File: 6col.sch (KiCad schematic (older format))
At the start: 47 parts, among them K1 KEYSW, K10 KEYSW, K11 KEYSW, K12 KEYSW, K13 KEYSW, K14 KEYSW, K15 KEYSW, K16 KEYSW, K17 KEYSW, K18 KEYSW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

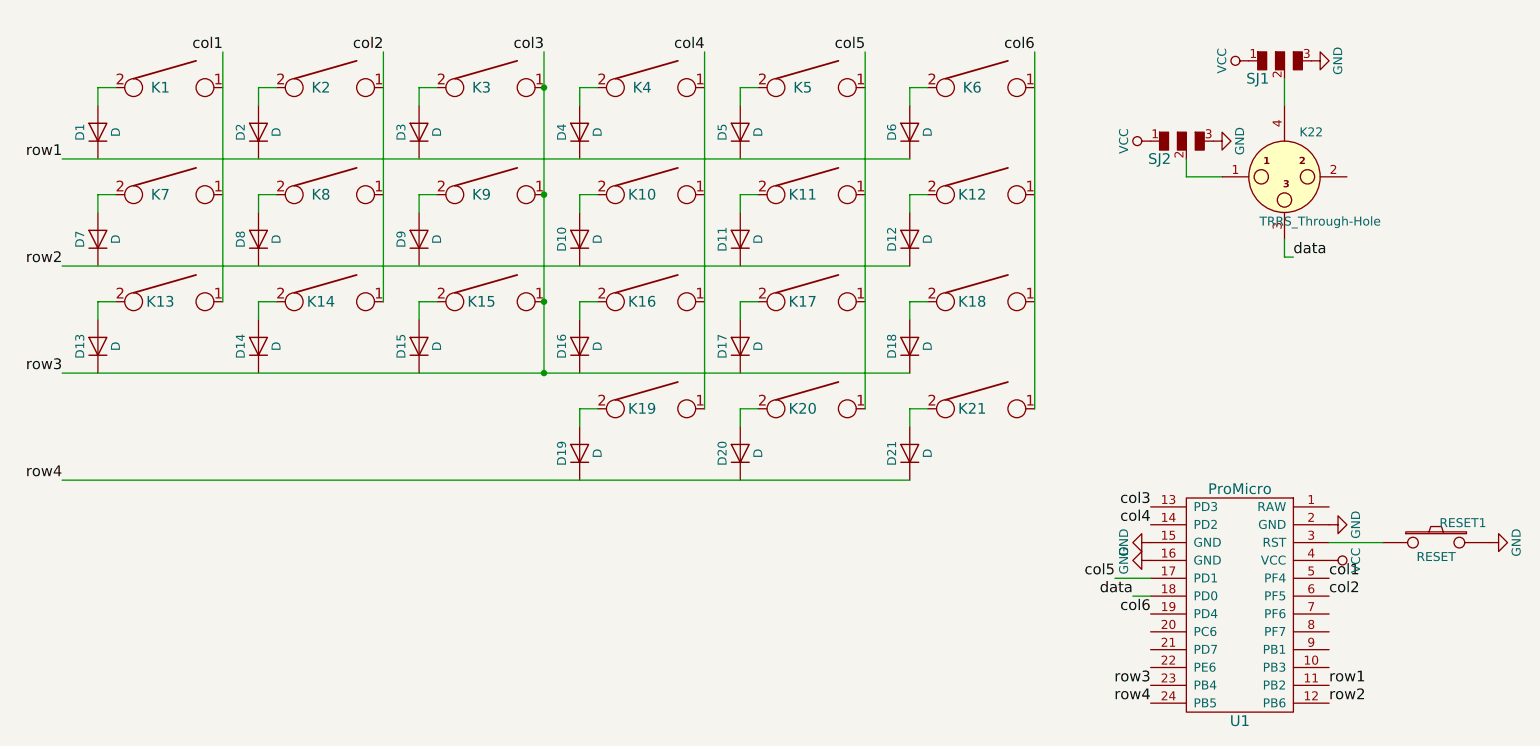
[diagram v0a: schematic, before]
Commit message: Fix short on sch between c3 and r3
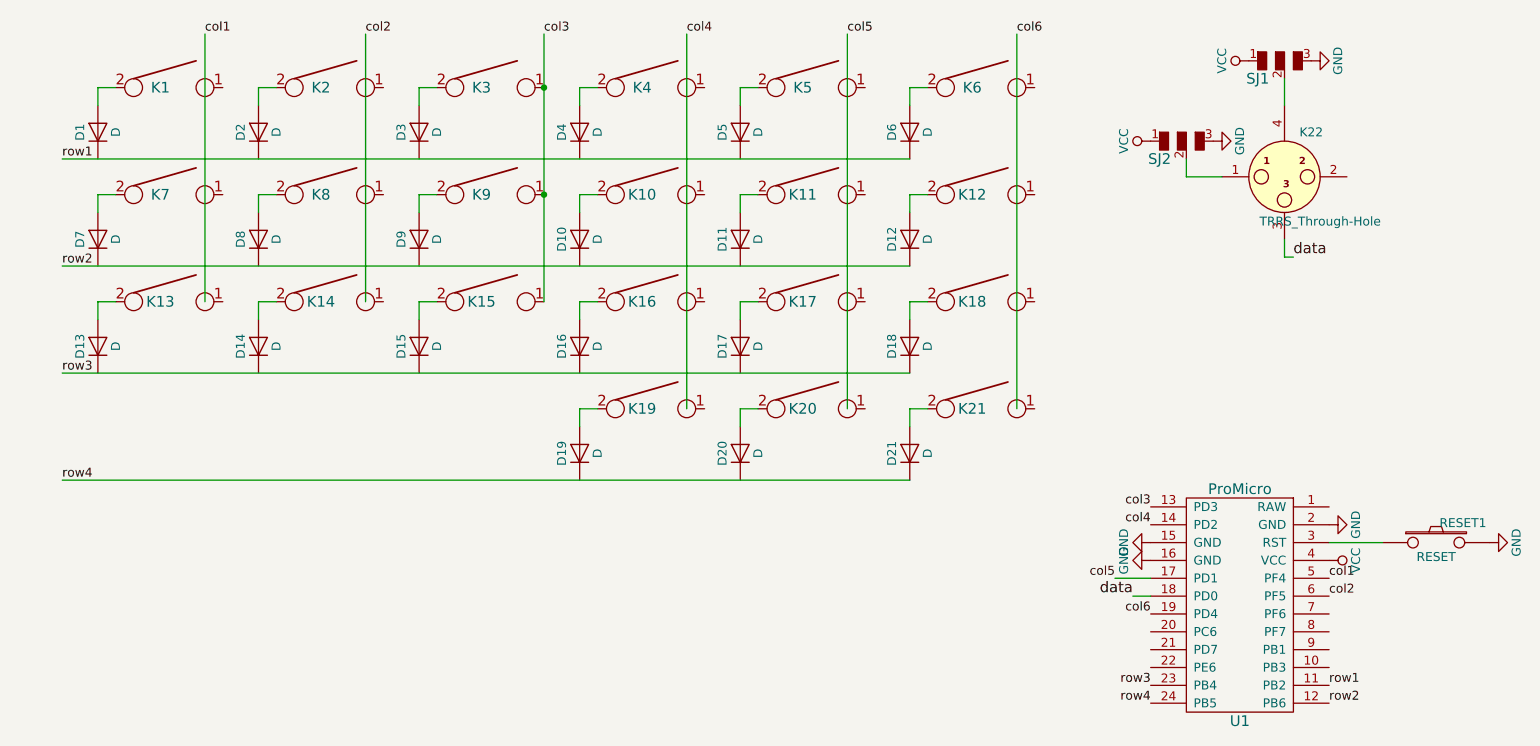
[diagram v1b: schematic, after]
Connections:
- wire segments 64 -> 62
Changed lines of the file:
@@
 $EndDescr
-$Comp
-L ProMicro:ProMicro U1
-U 1 1 588E2344
-P 8300 4650
-F 0 "U1" H 8300 3800 60  0000 C CNN
-F 1 "ProMicro" H 8300 5100 60  0000 C CNN
-F 2 "canadian_footprints:Pro_Micro" H 8300 4650 60  0001 C CNN
-F 3 "" H 8300 4650 60  0001 C CNN
-	1    8300 4650
-	1    0    0    -1
-$EndComp
 $Comp
 L canadian_parts:KEYSW K1
@@
 	0    -1   -1   0
 $EndComp
-Wire Wire Line
-	1900 2050 1900 1950
-Wire Wire Line
-	1900 1950 2000 1950
-Wire Wire Line
-	2800 2050 2800 1950
-Wire Wire Line
-	2800 1950 2900 1950
-Wire Wire Line
-	3700 2050 3700 1950
-Wire Wire Line
-	3700 1950 3800 1950
-Wire Wire Line
-	4600 2050 4600 1950
-Wire Wire Line
-	4600 1950 4700 1950
-Wire Wire Line
-	4600 2650 4600 2550
-Wire Wire Line
-	4600 2550 4700 2550
-Wire Wire Line
-	3700 2650 3700 2550
-Wire Wire Line
-	3700 2550 3800 2550
-Wire Wire Line
-	2800 2650 2800 2550
-Wire Wire Line
-	2800 2550 2900 2550
-Wire Wire Line
-	1900 2650 1900 2550
-Wire Wire Line
-	1900 2550 2000 2550
-Wire Wire Line
-	1900 3150 2000 3150
-Wire Wire Line
-	2800 3250 2800 3150
-Wire Wire Line
-	2800 3150 2900 3150
-Wire Wire Line
-	3700 3250 3700 3150
-Wire Wire Line
-	3700 3150 3800 3150
-Wire Wire Line
-	4600 3250 4600 3150
-Wire Wire Line
-	4600 3150 4700 3150
-Wire Wire Line
-	4600 3850 4600 3750
-Wire Wire Line
-	4600 3750 4700 3750
-Text Label 2600 1750 2    60   ~ 0
-col1
-Text Label 3500 1750 2    60   ~ 0
-col2
-Text Label 4400 1750 2    60   ~ 0
-col3
-Text Label 5300 1750 2    60   ~ 0
-col4
-Text Label 1700 2350 2    60   ~ 0
-row1
-Text Label 1700 2950 2    60   ~ 0
-row2
-Text Label 1700 3550 2    60   ~ 0
-row3
-Text Label 1700 4150 2    60   ~ 0
-row4
 $Comp
 L canadian_parts:SOLDER_JUMPER_3 SJ2
@@
 	1    0    0    -1
 $EndComp
-Wire Wire Line
-	8550 1900 8550 2050
-Wire Wire Line
-	8200 2450 8000 2450
-Wire Wire Line
-	8000 2450 8000 2350
 $Comp
 L power:GND #PWR01
@@
 Text Label 8600 2900 0    60   ~ 0
 data
-Wire Wire Line
-	8550 2800 8550 2900
-Wire Wire Line
-	8550 2900 8600 2900
 Text Label 7700 4800 2    60   ~ 0
 data
-Wire Wire Line
-	7700 4800 7800 4800
-Text Label 8800 4700 0    60   ~ 0
-col1
-Text Label 7800 4400 2    60   ~ 0
-col4
-Text Label 7600 4700 2    60   ~ 0
-col5
-Text Label 7800 4900 2    60   ~ 0
-col6
-Text Label 8800 5300 0    60   ~ 0
-row1
-Text Label 8800 5400 0    60   ~ 0
-row2
-Text Label 7800 5300 2    60   ~ 0
-row3
-Text Label 7800 5400 2    60   ~ 0
-row4
-Text Label 7800 4300 2    60   ~ 0
-col3
-Wire Wire Line
-	7600 4700 7800 4700
 $Comp
 L keyboard_parts:SW_PUSH RESET1
@@
 	0    -1   -1   0
 $EndComp
-Wire Wire Line
-	9100 4500 8800 4500
-Wire Wire Line
-	2600 1750 2600 3150
-Wire Wire Line
-	3500 1750 3500 3150
-Wire Wire Line
-	5300 1750 5300 3750
-Wire Wire Line
-	1900 3250 1900 3150
 $Comp
 L Device:D D13
@@
 	0    -1   -1   0
 $EndComp
-Text Label 8800 4800 0    60   ~ 0
-col2
-Wire Wire Line
-	6200 1750 6200 3750
-Text Label 6200 1750 2    60   ~ 0
-col5
-Wire Wire Line
-	5500 3750 5600 3750
-Wire Wire Line
-	5500 3850 5500 3750
-Wire Wire Line
-	5500 3150 5600 3150
-Wire Wire Line
-	5500 3250 5500 3150
-Wire Wire Line
-	5500 2550 5600 2550
-Wire Wire Line
-	5500 2650 5500 2550
-Wire Wire Line
-	5500 1950 5600 1950
-Wire Wire Line
-	5500 2050 5500 1950
 $Comp
 L Device:D D20
@@
 	1    0    0    -1
 $EndComp
-Wire Wire Line
-	7150 1750 7150 3750
-Text Label 7150 1750 2    60   ~ 0
-col6
-Wire Wire Line
-	6450 3750 6550 3750
-Wire Wire Line
-	6450 3850 6450 3750
-Wire Wire Line
-	6450 3150 6550 3150
-Wire Wire Line
-	6450 3250 6450 3150
-Wire Wire Line
-	6450 2550 6550 2550
-Wire Wire Line
-	6450 2650 6450 2550
-Wire Wire Line
-	6450 1950 6550 1950
-Wire Wire Line
-	6450 2050 6450 1950
 $Comp
 L Device:D D21
@@
 	1    0    0    -1
 $EndComp
-Wire Wire Line
-	1700 3550 4400 3550
-Wire Wire Line
-	1700 2950 6450 2950
-Wire Wire Line
-	1700 2350 6450 2350
-Wire Wire Line
-	1700 4150 6450 4150
-Wire Wire Line
-	4400 1750 4400 1950
-Connection ~ 4400 1950
-Wire Wire Line
-	4400 1950 4400 2550
-Connection ~ 4400 2550
-Wire Wire Line
-	4400 2550 4400 3150
-Connection ~ 4400 3150
-Wire Wire Line
-	4400 3150 4400 3550
-Connection ~ 4400 3550
-Wire Wire Line
-	4400 3550 6450 3550
 $Comp
 L canadian_parts:TRRS_Through-Hole K22
@@
 	1    0    0    -1
 $EndComp
+$Comp
+L ProMicro:ProMicro U1
+U 1 1 588E2344
+P 8300 4650
+F 0 "U1" H 8300 3800 60  0000 C CNN
+F 1 "ProMicro" H 8300 5100 60  0000 C CNN
+F 2 "canadian_footprints:Pro_Micro" H 8300 4650 60  0001 C CNN
+F 3 "" H 8300 4650 60  0001 C CNN
+	1    8300 4650
+	1    0    0    -1
+$EndComp
+Text Label 8800 5300 0    50   ~ 0
+row1
+Text Label 8800 5400 0    50   ~ 0
+row2
+Text Label 7800 5300 2    50   ~ 0
+row3
+Text Label 7800 5400 2    50   ~ 0
+row4
+Text Label 1700 2350 0    50   ~ 0
+row1
+Text Label 1700 2950 0    50   ~ 0
+row2
+Text Label 1700 3550 0    50   ~ 0
+row3
+Text Label 1700 4150 0    50   ~ 0
+row4
+Text Label 2500 1650 0    50   ~ 0
+col1
+Text Label 3400 1650 0    50   ~ 0
+col2
+Text Label 5200 1650 0    50   ~ 0
+col4
+Text Label 6100 1650 0    50   ~ 0
+col5
+Text Label 7050 1650 0    50   ~ 0
+col6
+Text Label 4400 1650 0    50   ~ 0
+col3
+Text Label 8800 4700 0    50   ~ 0
+col1
+Text Label 8800 4800 0    50   ~ 0
+col2
+Wire Wire Line
+	1900 2050 1900 1950
+Wire Wire Line
+	1900 1950 2000 1950
+Wire Wire Line
+	2800 2050 2800 1950
+Wire Wire Line
+	2800 1950 2900 1950
+Wire Wire Line
+	3700 2050 3700 1950
+Wire Wire Line
+	3700 1950 3800 1950
+Wire Wire Line
+	4600 2050 4600 1950
+Wire Wire Line
+	4600 1950 4700 1950
+Wire Wire Line
+	4600 2650 4600 2550
+Wire Wire Line
+	4600 2550 4700 2550
+Wire Wire Line
+	3700 2650 3700 2550
+Wire Wire Line
+	3700 2550 3800 2550
+Wire Wire Line
+	2800 2650 2800 2550
+Wire Wire Line
+	2800 2550 2900 2550
+Wire Wire Line
+	1900 2650 1900 2550
+Wire Wire Line
+	1900 2550 2000 2550
+Wire Wire Line
+	1900 3150 2000 3150
+Wire Wire Line
+	2800 3250 2800 3150
+Wire Wire Line
+	2800 3150 2900 3150
+Wire Wire Line
+	3700 3250 3700 3150
+Wire Wire Line
+	3700 3150 3800 3150
+Wire Wire Line
+	4600 3250 4600 3150
+Wire Wire Line
+	4600 3150 4700 3150
+Wire Wire Line
+	4600 3850 4600 3750
+Wire Wire Line
+	4600 3750 4700 3750
+Wire Wire Line
+	8550 1900 8550 2050
+Wire Wire Line
+	8200 2450 8000 2450
+Wire Wire Line
+	8000 2450 8000 2350
+Wire Wire Line
+	8550 2800 8550 2900
+Wire Wire Line
+	8550 2900 8600 2900
+Wire Wire Line
+	7700 4800 7800 4800
+Wire Wire Line
+	7600 4700 7800 4700
+Wire Wire Line
+	9100 4500 8800 4500
+Wire Wire Line
+	1900 3250 1900 3150
+Wire Wire Line
+	5500 3750 5600 3750
+Wire Wire Line
+	5500 3850 5500 3750
+Wire Wire Line
+	5500 3150 5600 3150
+Wire Wire Line
+	5500 3250 5500 3150
+Wire Wire Line
+	5500 2550 5600 2550
+Wire Wire Line
+	5500 2650 5500 2550
+Wire Wire Line
+	5500 1950 5600 1950
+Wire Wire Line
+	5500 2050 5500 1950
+Wire Wire Line
+	6450 3750 6550 3750
+Wire Wire Line
+	6450 3850 6450 3750
+Wire Wire Line
+	6450 3150 6550 3150
+Wire Wire Line
+	6450 3250 6450 3150
+Wire Wire Line
+	6450 2550 6550 2550
+Wire Wire Line
+	6450 2650 6450 2550
+Wire Wire Line
+	6450 1950 6550 1950
+Wire Wire Line
+	6450 2050 6450 1950
+Wire Wire Line
+	1700 2950 6450 2950
+Wire Wire Line
+	1700 2350 6450 2350
+Wire Wire Line
+	1700 4150 6450 4150
+Wire Wire Line
+	4400 1950 4400 2550
+Connection ~ 4400 2550
+Wire Wire Line
+	4400 2550 4400 3150
+Wire Wire Line
+	2500 3150 2500 1650
+Wire Wire Line
+	3400 3150 3400 1650
+Wire Wire Line
+	6100 3750 6100 1650
+Wire Wire Line
+	7050 3750 7050 1650
+Wire Wire Line
+	5200 3750 5200 1650
+Wire Wire Line
+	4400 1950 4400 1650
+Connection ~ 4400 1950
+Text Label 7800 4300 2    50   ~ 0
+col3
+Text Label 7800 4400 2    50   ~ 0
+col4
+Text Label 7600 4700 2    50   ~ 0
+col5
+Text Label 7800 4900 2    50   ~ 0
+col6
+Wire Wire Line
+	1700 3550 6450 3550
 $EndSCHEMATC

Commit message: Fix sch again
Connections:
- wire segments 62 -> 90
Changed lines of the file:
@@
 	1    0    0    -1
 $EndComp
-Text Label 8800 5300 0    50   ~ 0
+Text Label 7800 5300 2    60   ~ 0
+row3
+Text Label 1700 2350 2    60   ~ 0
 row1
-Text Label 8800 5400 0    50   ~ 0
+Text Label 1700 2950 2    60   ~ 0
 row2
-Text Label 7800 5300 2    50   ~ 0
+Text Label 1700 3550 2    60   ~ 0
 row3
-Text Label 7800 5400 2    50   ~ 0
+Text Label 1700 4150 2    60   ~ 0
 row4
-Text Label 1700 2350 0    50   ~ 0
+Text Label 2600 1650 0    60   ~ 0
+col1
+Text Label 3500 1650 0    60   ~ 0
+col2
+Text Label 5300 1650 0    60   ~ 0
+col4
+Text Label 6200 1650 0    60   ~ 0
+col5
+Text Label 7150 1650 0    60   ~ 0
+col6
+Text Label 4400 1650 0    60   ~ 0
+col3
+Wire Wire Line
+	1900 2050 1900 1950
+Wire Wire Line
+	1900 1950 2000 1950
+Wire Wire Line
+	2800 2050 2800 1950
+Wire Wire Line
+	2800 1950 2900 1950
+Wire Wire Line
+	3700 2050 3700 1950
+Wire Wire Line
+	3700 1950 3800 1950
+Wire Wire Line
+	4600 2050 4600 1950
+Wire Wire Line
+	4600 1950 4700 1950
+Wire Wire Line
+	4600 2650 4600 2550
+Wire Wire Line
+	4600 2550 4700 2550
+Wire Wire Line
+	3700 2650 3700 2550
+Wire Wire Line
+	3700 2550 3800 2550
+Wire Wire Line
+	2800 2650 2800 2550
+Wire Wire Line
+	2800 2550 2900 2550
+Wire Wire Line
+	1900 2650 1900 2550
+Wire Wire Line
+	1900 2550 2000 2550
+Wire Wire Line
+	1900 3150 2000 3150
+Wire Wire Line
+	2800 3250 2800 3150
+Wire Wire Line
+	2800 3150 2900 3150
+Wire Wire Line
+	3700 3250 3700 3150
+Wire Wire Line
+	3700 3150 3800 3150
+Wire Wire Line
+	4600 3250 4600 3150
+Wire Wire Line
+	4600 3150 4700 3150
+Wire Wire Line
+	4600 3850 4600 3750
+Wire Wire Line
+	4600 3750 4700 3750
+Wire Wire Line
+	8550 1900 8550 2050
+Wire Wire Line
+	8200 2450 8000 2450
+Wire Wire Line
+	8000 2450 8000 2350
+Wire Wire Line
+	8550 2800 8550 2900
+Wire Wire Line
+	8550 2900 8600 2900
+Wire Wire Line
+	7700 4800 7800 4800
+Wire Wire Line
+	7600 4700 7800 4700
+Wire Wire Line
+	9100 4500 8800 4500
+Wire Wire Line
+	1900 3250 1900 3150
+Wire Wire Line
+	5500 3750 5600 3750
+Wire Wire Line
+	5500 3850 5500 3750
+Wire Wire Line
+	5500 3150 5600 3150
+Wire Wire Line
+	5500 3250 5500 3150
+Wire Wire Line
+	5500 2550 5600 2550
+Wire Wire Line
+	5500 2650 5500 2550
+Wire Wire Line
+	5500 1950 5600 1950
+Wire Wire Line
+	5500 2050 5500 1950
+Wire Wire Line
+	6450 3750 6550 3750
+Wire Wire Line
+	6450 3850 6450 3750
+Wire Wire Line
+	6450 3150 6550 3150
+Wire Wire Line
+	6450 3250 6450 3150
+Wire Wire Line
+	6450 2550 6550 2550
+Wire Wire Line
+	6450 2650 6450 2550
+Wire Wire Line
+	6450 1950 6550 1950
+Wire Wire Line
+	6450 2050 6450 1950
+Wire Wire Line
+	1700 2950 1900 2950
+Wire Wire Line
+	1700 2350 1900 2350
+Wire Wire Line
+	1700 4150 4600 4150
+Text Label 7800 4300 2    60   ~ 0
+col3
+Text Label 7800 4400 2    60   ~ 0
+col4
+Text Label 7600 4700 2    60   ~ 0
+col5
+Text Label 7800 4900 2    60   ~ 0
+col6
+Wire Wire Line
+	1700 3550 1900 3550
+Wire Wire Line
+	7150 1650 7150 1950
+Wire Wire Line
+	6200 1650 6200 1950
+Wire Wire Line
+	3500 1650 3500 1950
+Wire Wire Line
+	2600 1650 2600 1950
+Text Label 7800 5400 2    60   ~ 0
+row4
+Text Label 8800 4700 0    60   ~ 0
+col1
+Text Label 8800 4800 0    60   ~ 0
+col2
+Text Label 8800 5300 0    60   ~ 0
 row1
-Text Label 1700 2950 0    50   ~ 0
+Text Label 8800 5400 0    60   ~ 0
 row2
-Text Label 1700 3550 0    50   ~ 0
-row3
-Text Label 1700 4150 0    50   ~ 0
-row4
-Text Label 2500 1650 0    50   ~ 0
-col1
-Text Label 3400 1650 0    50   ~ 0
-col2
-Text Label 5200 1650 0    50   ~ 0
-col4
-Text Label 6100 1650 0    50   ~ 0
-col5
-Text Label 7050 1650 0    50   ~ 0
-col6
-Text Label 4400 1650 0    50   ~ 0
-col3
-Text Label 8800 4700 0    50   ~ 0
-col1
-Text Label 8800 4800 0    50   ~ 0
-col2
-Wire Wire Line
-	1900 2050 1900 1950
-Wire Wire Line
-	1900 1950 2000 1950
-Wire Wire Line
-	2800 2050 2800 1950
-Wire Wire Line
-	2800 1950 2900 1950
-Wire Wire Line
-	3700 2050 3700 1950
-Wire Wire Line
-	3700 1950 3800 1950
-Wire Wire Line
-	4600 2050 4600 1950
-Wire Wire Line
-	4600 1950 4700 1950
-Wire Wire Line
-	4600 2650 4600 2550
-Wire Wire Line
-	4600 2550 4700 2550
-Wire Wire Line
-	3700 2650 3700 2550
-Wire Wire Line
-	3700 2550 3800 2550
-Wire Wire Line
-	2800 2650 2800 2550
-Wire Wire Line
-	2800 2550 2900 2550
-Wire Wire Line
-	1900 2650 1900 2550
-Wire Wire Line
-	1900 2550 2000 2550
-Wire Wire Line
-	1900 3150 2000 3150
-Wire Wire Line
-	2800 3250 2800 3150
-Wire Wire Line
-	2800 3150 2900 3150
-Wire Wire Line
-	3700 3250 3700 3150
-Wire Wire Line
-	3700 3150 3800 3150
-Wire Wire Line
-	4600 3250 4600 3150
-Wire Wire Line
-	4600 3150 4700 3150
-Wire Wire Line
-	4600 3850 4600 3750
-Wire Wire Line
-	4600 3750 4700 3750
-Wire Wire Line
-	8550 1900 8550 2050
-Wire Wire Line
-	8200 2450 8000 2450
-Wire Wire Line
-	8000 2450 8000 2350
-Wire Wire Line
-	8550 2800 8550 2900
-Wire Wire Line
-	8550 2900 8600 2900
-Wire Wire Line
-	7700 4800 7800 4800
-Wire Wire Line
-	7600 4700 7800 4700
-Wire Wire Line
-	9100 4500 8800 4500
-Wire Wire Line
-	1900 3250 1900 3150
-Wire Wire Line
-	5500 3750 5600 3750
-Wire Wire Line
-	5500 3850 5500 3750
-Wire Wire Line
-	5500 3150 5600 3150
-Wire Wire Line
-	5500 3250 5500 3150
-Wire Wire Line
-	5500 2550 5600 2550
-Wire Wire Line
-	5500 2650 5500 2550
-Wire Wire Line
-	5500 1950 5600 1950
-Wire Wire Line
-	5500 2050 5500 1950
-Wire Wire Line
-	6450 3750 6550 3750
-Wire Wire Line
-	6450 3850 6450 3750
-Wire Wire Line
-	6450 3150 6550 3150
-Wire Wire Line
-	6450 3250 6450 3150
-Wire Wire Line
-	6450 2550 6550 2550
-Wire Wire Line
-	6450 2650 6450 2550
-Wire Wire Line
-	6450 1950 6550 1950
-Wire Wire Line
-	6450 2050 6450 1950
-Wire Wire Line
-	1700 2950 6450 2950
-Wire Wire Line
-	1700 2350 6450 2350
-Wire Wire Line
-	1700 4150 6450 4150
+Connection ~ 1900 2350
+Wire Wire Line
+	1900 2350 2800 2350
+Connection ~ 2600 1950
+Wire Wire Line
+	2600 1950 2600 2550
+Connection ~ 2800 2350
+Wire Wire Line
+	2800 2350 3700 2350
+Connection ~ 3500 1950
+Wire Wire Line
+	3500 1950 3500 2550
+Connection ~ 3700 2350
+Wire Wire Line
+	3700 2350 4600 2350
+Wire Wire Line
+	4400 1650 4400 1950
 Wire Wire Line
 	4400 1950 4400 2550
+Connection ~ 4400 1950
+Connection ~ 4600 2350
+Wire Wire Line
+	4600 2350 5500 2350
+Wire Wire Line
+	5300 1650 5300 1950
+Connection ~ 5300 1950
+Wire Wire Line
+	5300 1950 5300 2550
+Connection ~ 5500 2350
+Wire Wire Line
+	5500 2350 6450 2350
+Connection ~ 6200 1950
+Wire Wire Line
+	6200 1950 6200 2550
+Connection ~ 7150 1950
+Wire Wire Line
+	7150 1950 7150 2550
+Connection ~ 7150 2550
+Wire Wire Line
+	7150 2550 7150 3150
+Connection ~ 7150 3150
+Wire Wire Line
+	7150 3150 7150 3750
+Connection ~ 6200 2550
+Wire Wire Line
+	6200 2550 6200 3750
+Connection ~ 5500 2950
+Wire Wire Line
+	5500 2950 6450 2950
+Connection ~ 5300 2550
+Wire Wire Line
+	5300 2550 5300 3750
+Connection ~ 4600 2950
+Wire Wire Line
+	4600 2950 5500 2950
 Connection ~ 4400 2550
 Wire Wire Line
 	4400 2550 4400 3150
-Wire Wire Line
-	2500 3150 2500 1650
-Wire Wire Line
-	3400 3150 3400 1650
-Wire Wire Line
-	6100 3750 6100 1650
-Wire Wire Line
-	7050 3750 7050 1650
-Wire Wire Line
-	5200 3750 5200 1650
-Wire Wire Line
-	4400 1950 4400 1650
-Connection ~ 4400 1950
-Text Label 7800 4300 2    50   ~ 0
-col3
-Text Label 7800 4400 2    50   ~ 0
-col4
-Text Label 7600 4700 2    50   ~ 0
-col5
-Text Label 7800 4900 2    50   ~ 0
-col6
-Wire Wire Line
-	1700 3550 6450 3550
+Connection ~ 3700 2950
+Wire Wire Line
+	3700 2950 4600 2950
+Connection ~ 3500 2550
+Wire Wire Line
+	3500 2550 3500 3150
+Connection ~ 2800 2950
+Wire Wire Line
+	2800 2950 3700 2950
+Connection ~ 2600 2550
+Wire Wire Line
+	2600 2550 2600 3150
+Connection ~ 1900 2950
+Wire Wire Line
+	1900 2950 2800 2950
+Connection ~ 1900 3550
+Wire Wire Line
+	1900 3550 2800 3550
+Connection ~ 2800 3550
+Wire Wire Line
+	2800 3550 3700 3550
+Connection ~ 3700 3550
+Wire Wire Line
+	3700 3550 4600 3550
+Connection ~ 4600 3550
+Wire Wire Line
+	4600 3550 5500 3550
+Connection ~ 5500 3550
+Wire Wire Line
+	5500 3550 6450 3550
+Connection ~ 5500 4150
+Wire Wire Line
+	5500 4150 6450 4150
+Connection ~ 4600 4150
+Wire Wire Line
+	4600 4150 5500 4150
 $EndSCHEMATC

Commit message: One more fix on sch
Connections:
- net col4: now also K16.1
- net col5: now also K17.1
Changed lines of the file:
@@
 Wire Wire Line
 	1700 2350 1900 2350
-Wire Wire Line
-	1700 4150 4600 4150
 Text Label 7800 4300 2    60   ~ 0
 col3
@@
 Connection ~ 6200 2550
 Wire Wire Line
-	6200 2550 6200 3750
+	6200 2550 6200 3150
 Connection ~ 5500 2950
 Wire Wire Line
@@
 Connection ~ 5300 2550
 Wire Wire Line
-	5300 2550 5300 3750
+	5300 2550 5300 3150
 Connection ~ 4600 2950
 Wire Wire Line
@@
 Wire Wire Line
 	5500 4150 6450 4150
-Connection ~ 4600 4150
+Wire Wire Line
+	1700 4150 4600 4150
 Wire Wire Line
 	4600 4150 5500 4150
+Connection ~ 4600 4150
+Connection ~ 5300 3150
+Wire Wire Line
+	5300 3150 5300 3750
+Connection ~ 6200 3150
+Wire Wire Line
+	6200 3150 6200 3750
 $EndSCHEMATC
